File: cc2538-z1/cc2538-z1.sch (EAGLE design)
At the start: 51 parts, among them U1 CC2538, U2 CC1120_RHM_32, X1 FA-128

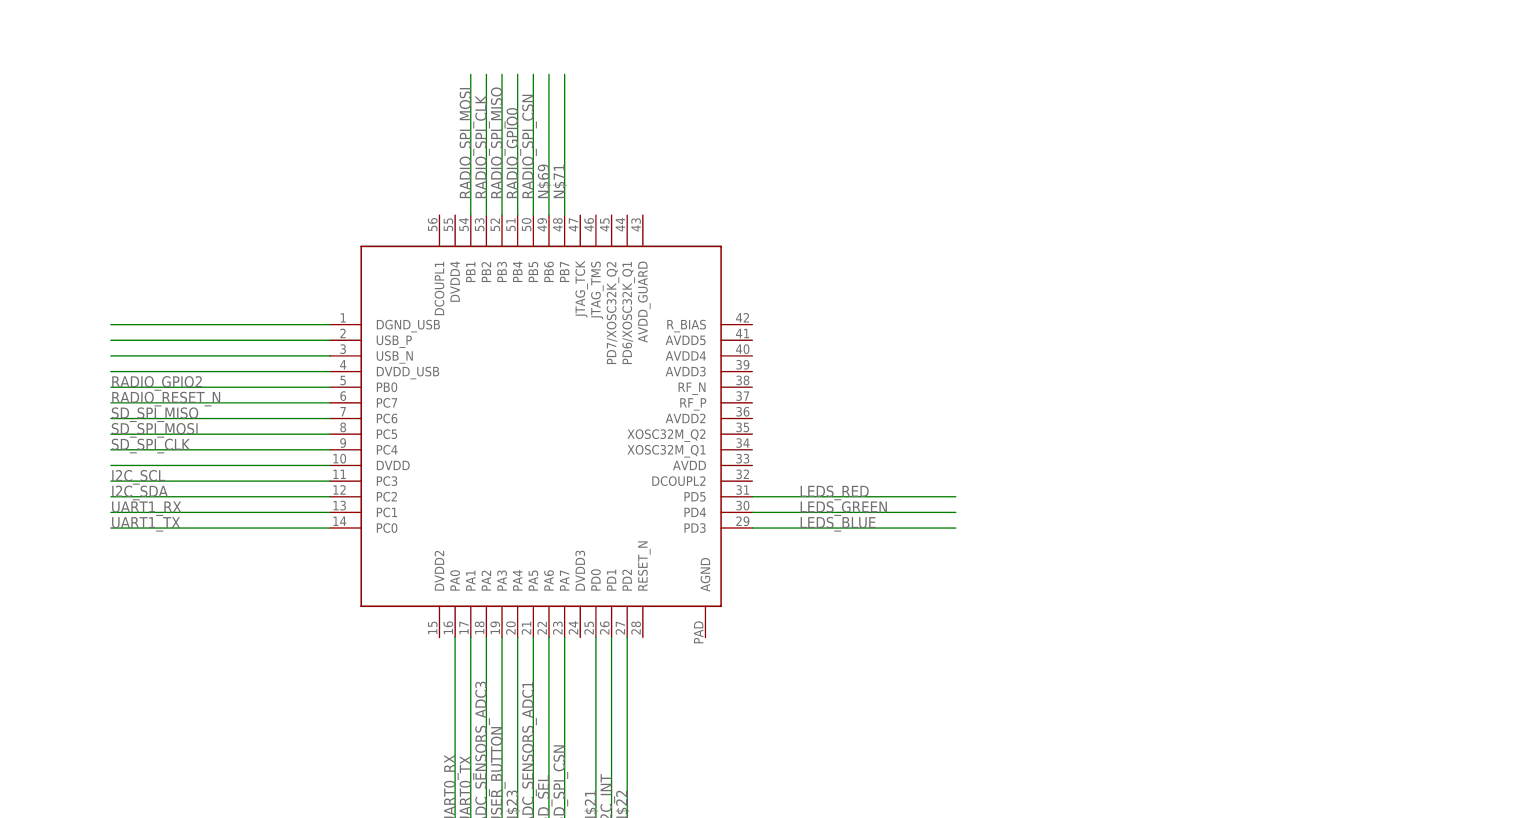
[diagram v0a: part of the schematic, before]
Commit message: Work on CC2538 board
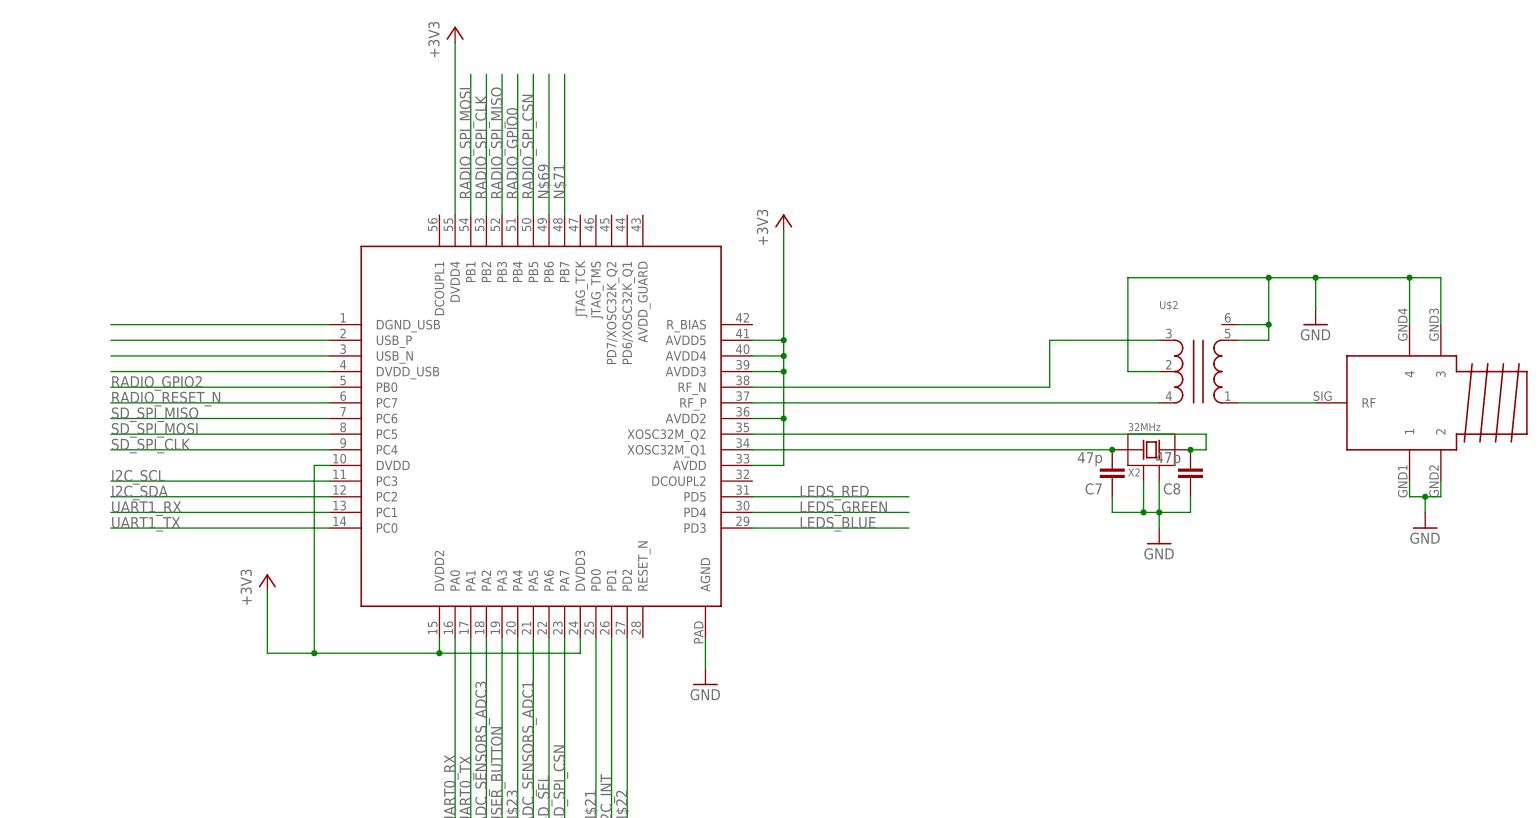
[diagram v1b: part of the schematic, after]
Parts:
- added C7, C8: 47p, rcl:C-EUC0603
- added U$1: SMATH, CC11x:SMATH
- added U$2: BALUN-2.4G, CC11x:BALUN-2.4G
- added X2: 32MHz, arm-cores:ABM8G-ABM8G
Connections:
- removed net N$70: U1.DVDD
- new net +3V3: U1.AVDD, U1.AVDD2, U1.AVDD3, U1.AVDD4, U1.AVDD5, U1.DVDD, U1.DVDD2, U1.DVDD3, U1.DVDD4
- new net 2.4G: U$1.RF, U$2.1
- new net 32M_Q1: C7.2, U1.XOSC32M_Q1, X2.1
- new net 32M_Q2: C8.2, U1.XOSC32M_Q2, X2.3
- new net N$28: U$2.4, U1.RF_P
- new net N$29: U$2.3, U1.RF_N
- net GND: now also C7.1, C8.1, U$1.1, U$1.2, U$1.3, U$1.4, U$2.2, U$2.5, U$2.6, U1.AGND, X2.2, X2.4

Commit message: CC2538 design work
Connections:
- net N$40 renamed ADC_1
- net N$41 renamed ADC_2
- net N$44 renamed DIGITAL_IO_2
- net N$46 renamed ADC_BATVOLTS
- net N$48 renamed DIGITAL_IO_1
- net N$51 renamed PWR_SENSE_EN
- net N$52 renamed PWR_RADIO_EN
- net N$55 renamed RS485_TXEN
- net N$57 renamed GPIO_INT_RAIN
- removed net N$53: H1.TB3
- removed net N$58: H1.CA3
- removed net N$59: H1.CA6
- removed net N$62: H1.D-3V
- net +3V3: now also H1.D-3V
- net RADIO_GPIO3: now also H1.TB3
- net RADIO_RESET_N: now also H1.CA6
- net RADIO_SPI_CSN: now also H1.CA3
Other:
- moved on the sheet: C7, C8, U$2, X2

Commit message: USB input layout done
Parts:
- removed C174, C175, C176, C177, C181, C191, C201: C_EU, CC11x:C_EU
- removed L172, L173, L174, L191, L192, L193, L201: L_US, CC11x:L_US
- added C1: 4.7uF, CC11x:C_EUC0603S
- added C2, C3: 1uF, CC11x:C_EUC0603S
- added C4: 0.1uF, CC11x:C_EUC0603S
- added J1: (no value), CC11x:47346-0001
- added L1: BALUN-2.4G, CC11x:BALUN-2.4G
- added L2, L3, L4: BEAD, CC11x:L_US0603
- added R10: (no value), rcl:R-EU_R0603
- added R9: 4.7k, rcl:R-EU_R0603
- added U3: TPD2E001IDRLRQ1, Texas Instruments_By_element14_Batch_1:TPD2E001IDRLRQ1
- added U4: CP2103, CC11x:CP2103
- C11, C121, C131, C151, C171, C172, C173, C211, C221, C231, C251, C261, C271, C281, C291, C301, C302, C311, C51, C61: value C_EU -> C_EU0402S; device CC11x:C_EU -> CC11x:C_EU0402S
- L171: value L_US -> L_US0402S; device CC11x:L_US -> CC11x:L_US0402S
- U$2: value BALUN-2.4G -> 0900PC15J0013; device CC11x:BALUN-2.4G -> CC11x:0900PC15J0013
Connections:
- net VDD renamed RVDD
- removed net N$34: H1.USB-5V
- removed net N$35: H1.D_P
- removed net N$36: H1.D_N
- removed net N$37: H1.USBGND
- new net +3V3_SERIAL: C1.1, C3.1, C4.1, R9.2, U4.VDD, U4.VIO
- new net +5V: C2.2, L2.2, U4.VBUS, U4.VREGIN
- new net +5V_USB: H1.USB-5V, J1.1, L2.1, U3.VCC
- new net BSL_DTR: U4.DTR
- new net BSL_RTS: U4.RTS
- new net GNDA: H1.USBGND, J1.5, L3.1, R10.1, U3.GND
- new net N$20: J1.4, R10.2
- new net N$26: U4.GPIO_2
- new net N$27: R9.1, U4.NRESET
- new net N$30: U4.GPIO_3
- new net RGND: ANT_868.1, ANT_868.2, ANT_868.3, ANT_868.4, C11.2, C121.2, C131.2, C151.2, C171.2, C172.2, C211.2, C221.2, C251.2, C261.2, C271.2, C281.2, C291.2, C301.2, C302.2, C311.2, C51.2, C61.2, L4.1, R12.1, R12.2, R141.1, U$2.GND, U2.EPAD, U2.EXT_XOSC, X1.2, X1.4
- new net USB_D_N: H1.D_N, J1.2, U3.IO1, U4.D-
- new net USB_D_P: H1.D_P, J1.3, U3.IO2, U4.D+
- net 2.4G: now also L1.1; no longer U$2.1
- net GND: now also C1.2, C2.1, C3.2, C4.2, L1.2, L1.5, L1.6, L3.2, L4.2, U4.GND; no longer ANT_868.1, ANT_868.2, C11.2, C121.2, C131.2, C151.2, C171.2, C172.2, C175.2, C201.2, C211.2, C221.2, C251.2, C261.2, C271.2, C281.2, C291.2, C301.2, C302.2, C311.2, C51.2, C61.2, L192.2, R12.1, R12.2, R141.1, U$2.2, U$2.5, U$2.6, U2.EPAD, U2.EXT_XOSC, X1.2, X1.4
- net N$10: now also U$2.LNA_P; no longer C191.1, L191.2, L192.1
- net N$11: now also ANT_868.RF, U$2.ANT; no longer C191.2, L193.1, L201.2
- net N$12: now also U$2.TRX; no longer C181.1, L193.2
- net N$14: now also U$2.PA; no longer C174.1
- net N$15: now also U4.GPIO_0; no longer C174.2, C176.1, L172.1
- net N$16: now also U4.DSR; no longer C176.2, C181.2, L172.2, L173.1
- net N$17: now also U4.GPIO_1; no longer C175.1, C177.1, L173.2, L174.1
- net N$18: now also U4.CTS; no longer ANT_868.RF, C177.2, L174.2
- net N$28: now also L1.4; no longer U$2.4
- net N$29: now also L1.3; no longer U$2.3
- net N$9: now also U$2.LNA_N; no longer C201.1, L191.1, L201.1
- net UART0_RX: now also U4.TXD
- net UART0_TX: now also U4.RXD
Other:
- moved on the sheet: C171, C172, C173, L171, R171

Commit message: Added Radio power filtering & switch.
I need to stop committing at 6am...
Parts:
- added C5, C6: 100nf, CC11x:C_EUC0603S
- added F2: BALUN-2.4G, CC11x:BALUN-2.4G
- added Q2: DMG6602SVT, farnell-parts:DMG6602SVT
- added R11, R13: 100K, resistor:R-EU_R0805
- L1: value BALUN-2.4G -> BEAD; device CC11x:BALUN-2.4G -> CC11x:L_US0603
- renumbered U$2 to F1
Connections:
- new net N$31: C6.1, L1.1, Q2G$2.D
- new net N$34: Q2G$1.D@1, Q2G$2.G, R11.1
- net +3V3: now also Q2G$2.S, R11.2
- net 2.4G: now also F2.1; no longer L1.1
- net GND: now also C6.2, F2.2, F2.5, F2.6, Q2G$1.S, R13.1; no longer L1.2, L1.5, L1.6
- net N$28: now also F2.4; no longer L1.4
- net N$29: now also F2.3; no longer L1.3
- net PWR_RADIO_EN: now also Q2G$1.G, R13.2
- net RGND: now also C5.2
- net RVDD: now also C5.1, L1.2
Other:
- moved on the sheet: L4

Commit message: Board check in before placing & routing CPU
Added CC1120/1200 ref chunk

Added partslist with Farnell links
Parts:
- removed U$1: SMATH, CC11x:SMATH
- added C10, C9: 1uF, rcl:C-EUC0603
- added C12, C13: 47p, rcl:C-EUC0603
- added H4: FTS-105-01-L-D, CC11x:FTS-105-01-L-D
- added R14: 100k, rcl:R-EU_R0603
- added R15: DNP, rcl:R-EU_R0603
- added R16: (no value), rcl:R-EU_R0603
- added R17: 56k, rcl:R-EU_R0603
- added SD1: MICRO_SD-SPI-MOLEX_503182-0853, glacsweb:MICRO_SD-SPI-MOLEX_503182-0853
- added X3: 32.768K, arm-cores:ABS07
- R9: value 4.7k -> 10k
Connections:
- removed net ADC_1: H1.ADC1
- removed net ADC_2: H1.ADC2
- removed net ADC_BATVOLTS: H1.ADC7
- removed net I2C_INT: U1.PD1
- removed net N$22: U1.PD2
- removed net N$23: U1.PA4
- removed net N$24: H1.USER_INT
- removed net N$25: H1.ALERT
- removed net N$32: H1.UCBICLK
- removed net N$33: H1.TBCLK
- removed net N$39: H1.ADC0
- removed net N$42: H1.ADC3
- removed net N$43: H1.ADC4
- removed net N$45: H1.ADC6
- removed net N$49: H1.TA1
- removed net N$50: H1.TA2
- removed net N$54: H1.CAOUT
- removed net N$56: H1.CA1
- removed net N$60: H1.BSL_TX
- removed net N$61: H1.BSL_RX
- removed net N$69: U1.PB6
- removed net N$71: U1.PB7
- new net 32K_Q1: C12.2, U1.PD7/XOSC32K_Q2, X3.3
- new net 32K_Q2: C13.2, U1.PD6/XOSC32K_Q1, X3.1
- new net ADC_SENSORS_ADC2: H1.ADC2, U1.PA4
- new net CC2538_NRESET: H4.10, U1.RESET_N
- new net DCOUPL: C10.2, C9.2, U1.DCOUPL1, U1.DCOUPL2
- new net JTAG_TCK: H4.4, U1.JTAG_TCK
- new net JTAG_TDI: H4.8
- new net JTAG_TMS: H4.2, H4.6, U1.JTAG_TMS
- net +3V3: now also H4.1, R15.2, SD1.DETECT, U1.AVDD_GUARD
- net 2.4G: no longer U$1.RF
- net ADC_SENSORS_ADC1: now also H1.ADC1
- net ADC_SENSORS_ADC3: now also H1.ADC7
- net DIGITAL_IO_1: now also U1.PB7
- net DIGITAL_IO_2: now also U1.PB6
- net GND: now also C10.1, C12.1, C13.1, C9.1, H4.3, H4.5, R14.2, R17.2, SD1.VSS; no longer U$1.1, U$1.2, U$1.3, U$1.4
- net N$21: now also R17.1, U1.R_BIAS; no longer U1.PD0
- net PWR_RADIO_EN: now also U1.PD2
- net PWR_SENSE_EN: now also U1.PD1
- net RADIO_GPIO2: now also H1.TB3
- net RADIO_GPIO3: no longer H1.TB3
- net RS485_TXEN: now also U1.PD0
- net SD_SEL: now also R14.1, R15.1, R16.1, R16.2, SD1.SWITCH, SD1.VDD
- net SD_SPI_CLK: now also SD1.SCLK
- net SD_SPI_CSN: now also SD1.CS
- net SD_SPI_MISO: now also SD1.DO
- net SD_SPI_MOSI: now also SD1.DI
- net UART0_RX: now also H1.BSL_RX
- net UART0_TX: now also H1.BSL_TX
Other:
- moved on the sheet: C5, C6, L1, L4, R13

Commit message: PCB routing attempt 1
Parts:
- added ANT: UFL, CC11x:UFL
- added C14, C15: 1uF, CC11x:C_EUC0603S
- added J2: 2-PIN-MOLEX, farnell-parts:2-PIN-MOLEX
- added LED: CLV1A-FKB-CJ1M1F1BB7R4S3, CC11x:CLV1A-FKB-CJ1M1F1BB7R4S3
- added R18, R19: 100k, rcl:R-EU_R0603
- added R20, R21, R22: 220, rcl:R-EU_R0603
- added R23, R24, R25: 4.7K, rcl:R-EU_R0603
- added R26, R27: 4.7k, rcl:R-EU_R0603
- added RST, USR: KMR2X1G, CC11x:KMR2X1G
- added U5, U6, U7: BSS138PS, CC11x:BSS138PS
- R7: value (none) -> 220
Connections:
- removed net DIGITAL_IO_1: H1.TA0, U1.PB7
- removed net DIGITAL_IO_2: H1.ADC5, U1.PB6
- removed net JTAG_TDI: H4.8
- new net JTAG_TDI/DIO2: H1.ADC5, H4.8, U1.PB6
- new net JTAG_TDO/DIO1: H1.TA0, H4.6, U1.PB7
- new net N$22: LED.1, R20.2
- new net N$23: LED.3, R21.2
- new net N$24: LED.4, R22.2
- new net N$25: R20.1, U5.D1
- new net N$32: R21.1, U6.D1
- new net N$33: R22.1, U5.D2
- net +3V3: now also J2.1, J2.2, LED.2, R18.2, R19.2
- net 2.4G: now also ANT.RF
- net BSL_DTR: now also R27.2, U7.G1
- net BSL_RTS: now also R26.2, U7.G2
- net CC2538_NRESET: now also C14.1, R18.1, RST.1, U7.D2
- net GND: now also ANT.1, ANT.2, C14.2, C15.2, H4.9, R23.2, R24.2, R25.2, R26.1, R27.1, RST.2, RST.3, U5.S1, U5.S2, U6.S1, U7.S1, U7.S2, USR.2, USR.3
- net JTAG_TMS: no longer H4.6
- net LEDS_BLUE: now also R25.1, U6.G1
- net LEDS_GREEN: now also R24.1, U5.G2
- net LEDS_RED: now also R23.1, U5.G1
- net RADIO_GPIO3: no longer R7.1, R7.2
- net USER_BUTTON: now also C15.1, R19.1, U7.D1, USR.1

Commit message: 48 airwires left.
Still need to finalise SD sel setup.

May need to swap to a 4-layer board.

What am I doing working on PCBs at 8 am?
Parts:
- removed R7: 220, rcl:R-EU_R0603
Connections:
- net RADIO_GPIO0: now also H1.CAOUT
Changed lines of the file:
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@@
 <part name="+3V10" library="supply1" deviceset="+3V3" device=""/>
 <part name="GND22" library="supply1" deviceset="GND" device=""/>
-<part name="R7" library="rcl" deviceset="R-EU_" device="R0603" value="220"/>
 <part name="R23" library="rcl" deviceset="R-EU_" device="R0603" value="4.7K"/>
 <part name="R24" library="rcl" deviceset="R-EU_" device="R0603" value="4.7K"/>
@@
 <instance part="X3" gate="A" x="304.8" y="165.1"/>
 <instance part="ANT" gate="A" x="378.46" y="104.14"/>
-<instance part="R7" gate="G$1" x="401.32" y="137.16" rot="R90"/>
 <instance part="U7" gate="A" x="477.52" y="220.98" smashed="yes">
 <attribute name="NAME" x="485.5972" y="231.0384" size="2.0828" layer="95" ratio="10" rot="SR0"/>
@@
 <label x="261.62" y="137.16" size="1.778" layer="95" rot="R90"/>
 </segment>
-</net>
+<segment>
+<pinref part="H1" gate="G$1" pin="CAOUT"/>
+<wire x1="7.62" y1="86.36" x2="-22.86" y2="86.36" width="0.1524" layer="91"/>
+<label x="-22.86" y="86.36" size="1.778" layer="95"/>
+</segment>
+</net>
